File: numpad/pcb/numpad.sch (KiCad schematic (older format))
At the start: 46 parts, among them J1 USB_C_Receptacle_USB2.0, U1 ATmega32U4-AU, Y1 Crystal_GND24_Small

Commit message: serpated schematic into multisheet and reset annotation in sheet_num*1000
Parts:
- removed C1: 1uF, symbol Device:C
- removed C2, C3: C, symbol Device:C
- removed C4, C5, C6, C7, C8: 0.1uF, symbol Device:C
- removed D1, D10, D11, D12, D13, D14, D15, D16, D17, D2, D3, D4, D5, D6, D7, D8, D9: BAT42W-V, Diode_SMD:D_SOD-123, symbol Diode:BAT42W-V
- removed F1: 500m, symbol Device:Polyfuse_Small
- removed J1: USB_C_Receptacle_USB2.0, symbol Connector:USB_C_Receptacle_USB2.0
- removed MX1, MX10, MX11, MX12, MX13, MX14, MX15, MX2, MX3, MX4, MX6, MX7, MX8, MX9: MX-NoLED, keyboard:MX-1U-NoLED, symbol keyboard:MX-NoLED
- removed MX16, MX17, MX5: MX-NoLED, keyboard:MX-2U-NoLED, symbol keyboard:MX-NoLED
- removed U1: ATmega32U4-AU, Package_QFP:TQFP-44_10x10mm_P0.8mm, symbol MCU_Microchip_ATmega:ATmega32U4-AU
- removed Y1: Crystal_GND24_Small, symbol Device:Crystal_GND24_Small
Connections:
- net labels removed: 5v_post_fuse, GND, IC_XTAL1, IC_XTAL2, column_0, column_1, column_2, column_3, row_0, row_1, row_2, row_3, row_4, usb_d_N, usb_d_P
- wire segments 117 -> 0
- no-connect marks 2 -> 0
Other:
- note removed: "Crystal Oscilliator"
- note removed: "Decoupling Resistor"
- note removed: "Keyboard Matrix"
- note removed: "Microcontroller"
- note removed: "USB C 2.0"

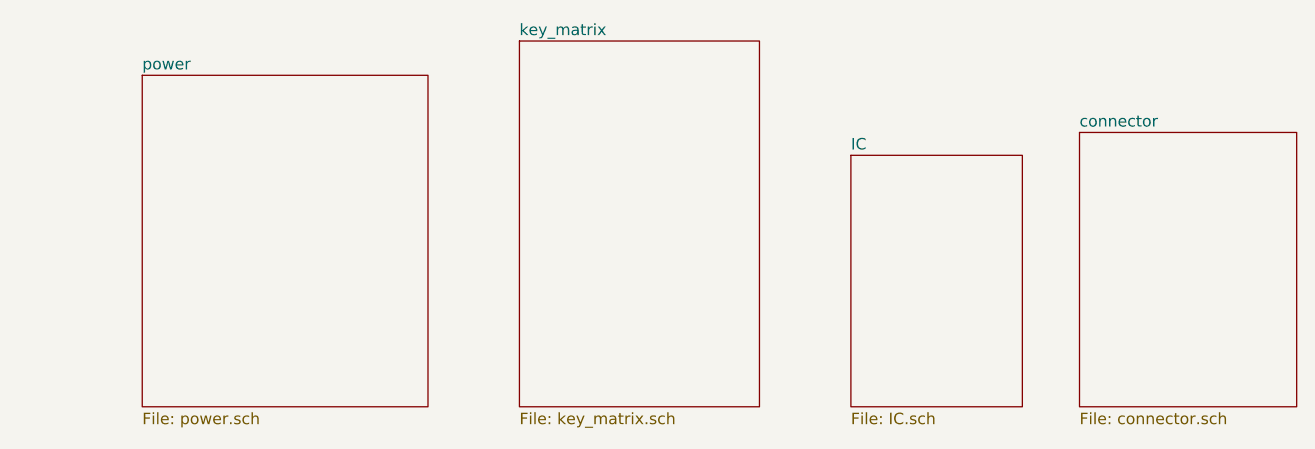
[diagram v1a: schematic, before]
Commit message: updated all net label and connected the sheet pins
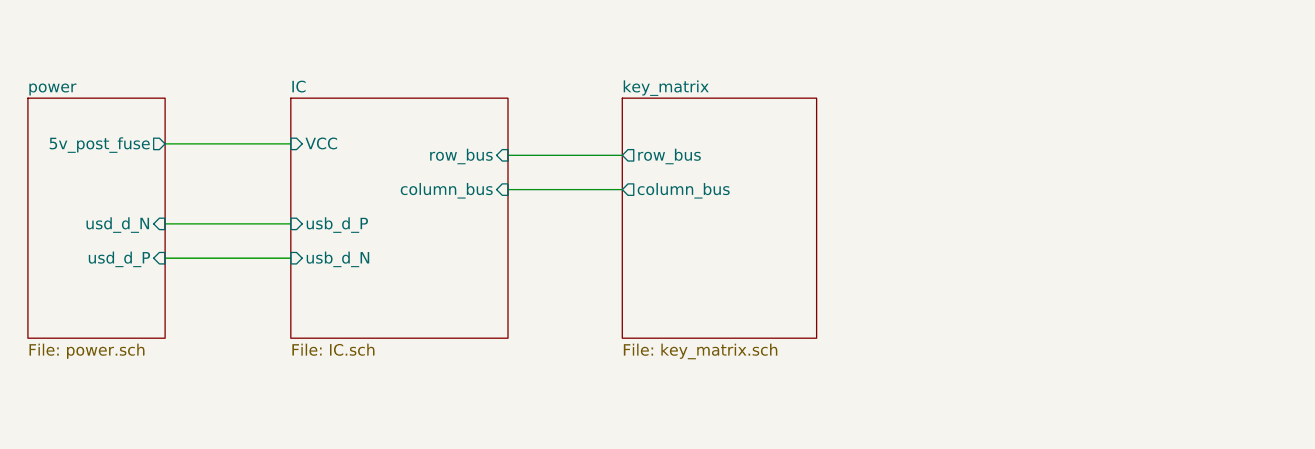
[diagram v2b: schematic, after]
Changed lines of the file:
@@
 $Descr A4 11693 8268
 encoding utf-8
-Sheet 1 5
+Sheet 1 4
 Title ""
 Date ""
@@
 $EndDescr
 $Sheet
-S 3550 1350 1050 1600
+S 2550 1600 950  1050
+U 61388DBF
+F0 "IC" 50
+F1 "IC.sch" 50
+F2 "row_bus" I R 3500 1850 50
+F3 "column_bus" I R 3500 2000 50
+F4 "VCC" I L 2550 1800 50
+F5 "usb_d_P" I L 2550 2150 50
+F6 "usb_d_N" I L 2550 2300 50
+$EndSheet
+$Sheet
+S 1400 1600 600  1050
+U 613B1F02
+F0 "power" 50
+F1 "power.sch" 50
+F2 "5v_post_fuse" O R 2000 1800 50
+F3 "usd_d_N" I R 2000 2150 50
+F4 "usd_d_P" I R 2000 2300 50
+$EndSheet
+Wire Wire Line
+	2000 1800 2550 1800
+Wire Wire Line
+	2000 2150 2550 2150
+Wire Wire Line
+	2000 2300 2550 2300
+$Sheet
+S 4000 1600 850  1050
 U 6138874F
 F0 "key_matrix" 50
 F1 "key_matrix.sch" 50
+F2 "row_bus" O L 4000 1850 50
+F3 "column_bus" O L 4000 2000 50
 $EndSheet
-$Sheet
-S 5000 1850 750  1100
-U 61388DBF
-F0 "IC" 50
-F1 "IC.sch" 50
-$EndSheet
-$Sheet
-S 6000 1750 950  1200
-U 613893FD
-F0 "connector" 50
-F1 "connector.sch" 50
-$EndSheet
-$Sheet
-S 1900 1500 1250 1450
-U 613B1F02
-F0 "power" 50
-F1 "power.sch" 50
-$EndSheet
+Wire Wire Line
+	3500 1850 4000 1850
+Wire Wire Line
+	3500 2000 4000 2000
 $EndSCHEMATC
